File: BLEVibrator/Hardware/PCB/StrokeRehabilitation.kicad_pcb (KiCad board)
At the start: 2 copper layers, 38 x 45 mm, 17 parts, among them P1 JST_PH_01x02, P2 CONN_01X05, Q1 MOSFET_N, SW1 SWITCH_DPDT, U1 TPS737, U2 RFD22301, U3 Brushed_DC_motor

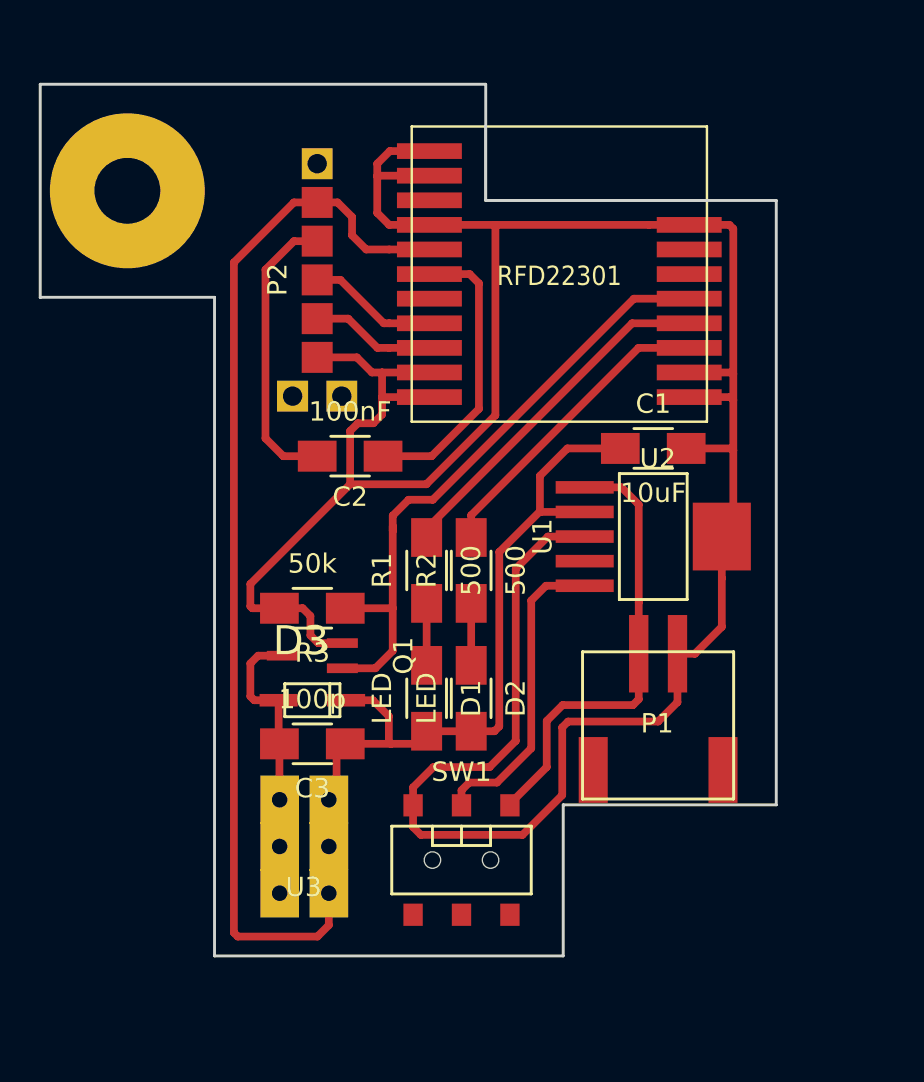
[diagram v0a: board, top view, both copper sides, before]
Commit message: Updated the PCB to have a side-mounted slide switch and connection status LED. The case still needs to be updated to match
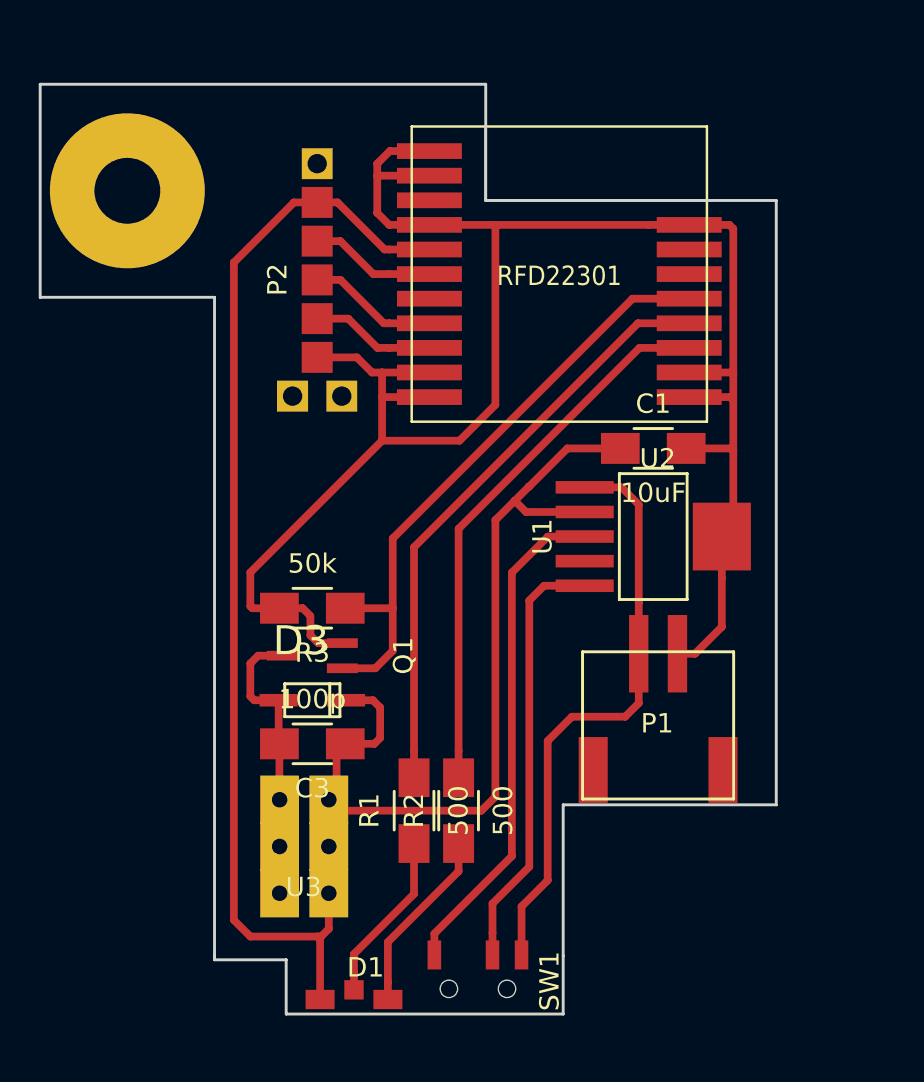
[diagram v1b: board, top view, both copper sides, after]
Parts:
- removed C2: 100nF, FabLibrary:C_1206_HandSoldering_IainEdit
- removed D2: LED, FabLibrary:C_1206_HandSoldering_IainEdit
- D1: value LED -> BI_LED_common_anode; footprint FabLibrary:C_1206_HandSoldering_IainEdit -> IainPersonalLibrary:Bi_LED_SM1204BC-RG
- SW1: value SWITCH_DPDT -> SWITCH_INV; footprint IainPersonalLibrary:SlideSwitch_AYZ0202AGRLC -> IainPersonalLibrary:SlideSwitch_SSSS810701
- moved D1 16.0 mm to (144.8, 146.8), turned to 0 degrees
- moved R1 12.4 mm to (147.8, 137.0)
- moved R2 12.4 mm to (150.2, 137.0)
- moved SW1 6.70 mm to (151.2, 146.2), turned to 0 degrees
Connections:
- D1 pad 1: Net-(D1-Pad1) -> VDD
- D1 pad 2: VDD -> Net-(D1-Pad2)
- P1 pad 1: Net-(C4-Pad2) -> Net-(P1-Pad1)
- P2 pad 2: Net-(C2-Pad2) -> Net-(P2-Pad2)
- R1 pad 1: Net-(D1-Pad1) -> Net-(D1-Pad2)
- R2 pad 1: Net-(D2-Pad1) -> Net-(D1-Pad3)
- SW1 pad 1: Net-(SW1-Pad1) -> GND
- SW1 pad 3: Net-(SW1-Pad3) -> Net-(P1-Pad1)
- U1 pad 1: Net-(C4-Pad2) -> Net-(P1-Pad1)
- U1 pad 5: Net-(SW1-Pad5) -> Net-(SW1-Pad2)
- U2 pad P$14: Net-(C2-Pad1) -> Net-(P2-Pad2)
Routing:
- net Net-(P1-Pad1): track 0.00 -> 30.5 mm
- net Net-(C4-Pad2): track 23.6 -> 0.00 mm
- net Net-(SW1-Pad2): track 0.00 -> 22.3 mm
- net GND: track 150.8 -> 130.7 mm
- net Net-(SW1-Pad5): track 16.0 -> 0.00 mm
- net Net-(C2-Pad1): track 15.2 -> 0.00 mm
- net Net-(C2-Pad2): track 15.0 -> 0.00 mm
- net Net-(R2-Pad2): track 16.0 -> 28.6 mm
- net Net-(R1-Pad2): track 18.4 -> 30.9 mm
- net VDD: track 96.3 -> 106.4 mm
- net Net-(D1-Pad3): track 0.00 -> 9.56 mm
- net Net-(D1-Pad2): track 0.00 -> 8.83 mm
- net Net-(P2-Pad2): track 0.00 -> 6.50 mm
- net Net-(D2-Pad1): track 3.20 -> 0.00 mm
- net Net-(D1-Pad1): track 3.20 -> 0.00 mm
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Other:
- board size 38 x 45 mm -> 38 x 48 mm
- board text added: "GND internally connected in TPS737"

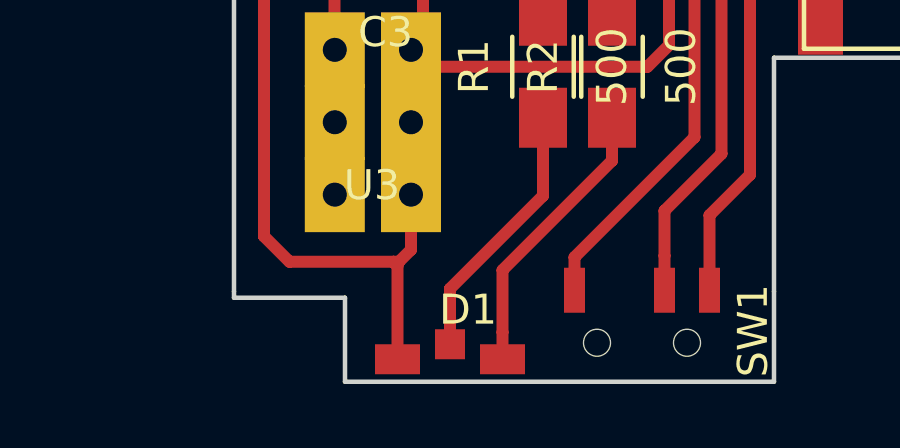
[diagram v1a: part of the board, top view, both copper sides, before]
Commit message: Moved side mount LED back a little bit to make placement and soldering easier
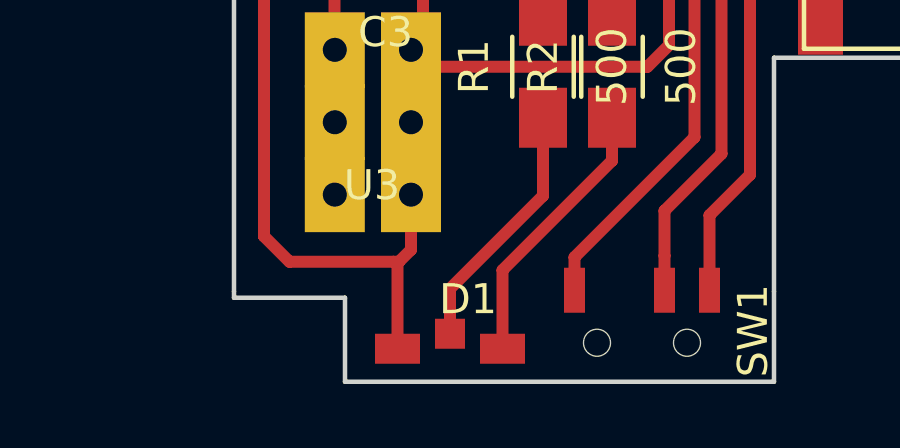
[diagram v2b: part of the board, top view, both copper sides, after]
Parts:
- moved D1 0.35 mm to (144.8, 146.4)
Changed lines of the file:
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@@
     (links 41)
     (no_connects 1)
-    (area 128.474999 99.424999 166.625001 147.575001)
+    (area 128.474999 98.33338 183.342857 151.275)
     (thickness 1.6)
     (drawings 29)
-    (tracks 156)
+    (tracks 154)
     (zones 0)
     (modules 15)
@@
   )
   (module IainPersonalLibrary:Bi_LED_SM1204BC-RG (layer F.Cu)
-    (at 144.75 146.75)
+    (at 144.75 146.4)
     (fp_text reference D1 (at 0.6 -1.65) (layer F.SilkS)
       (effects (font (size 1 1) (thickness 0.15)))
@@
   (gr_line (start 137.55 110.5) (end 128.55 110.5) (angle 90) (layer Edge.Cuts) (width 0.15))
   (gr_line (start 137.55 144.5) (end 137.55 110.5) (angle 90) (layer Edge.Cuts) (width 0.15))
+  (segment (start 143 146.4) (end 143 143.55) (width 0.4) (layer F.Cu) (net 1))
+  (segment (start 143 143.55) (end 143.05 143.5) (width 0.4) (layer F.Cu) (net 1))
   (segment (start 153.05 121) (end 152.05 122) (width 0.4) (layer F.Cu) (net 1))
   (segment (start 152.05 122) (end 152.05 136.280002) (width 0.4) (layer F.Cu) (net 1))
@@
   (segment (start 143.45 143.1) (end 143.05 143.5) (width 0.4) (layer F.Cu) (net 1))
   (segment (start 143.05 143.5) (end 142.863 143.5) (width 0.4) (layer F.Cu) (net 1))
-  (segment (start 142.863 143.5) (end 143 143.637) (width 0.4) (layer F.Cu) (net 1))
-  (segment (start 143 143.637) (end 143 146.75) (width 0.4) (layer F.Cu) (net 1))
   (segment (start 144.3 133.55) (end 145.8 133.55) (width 0.4) (layer F.Cu) (net 1))
   (segment (start 145.8 133.55) (end 146.1 133.25) (width 0.4) (layer F.Cu) (net 1))
@@
   (segment (start 158.56 120.31) (end 156.66 120.31) (width 0.4) (layer F.Cu) (net 15))
   (segment (start 159.45 126.25) (end 159.45 128.9) (width 0.4) (layer F.Cu) (net 15))
-  (segment (start 146.5 145.85) (end 146.5 146.75) (width 0.4) (layer F.Cu) (net 16))
-  (segment (start 146.5 143.781386) (end 146.5 145.85) (width 0.4) (layer F.Cu) (net 16))
+  (segment (start 146.5 143.781386) (end 146.5 146.4) (width 0.4) (layer F.Cu) (net 16))
   (segment (start 150.15 140.131386) (end 146.5 143.781386) (width 0.4) (layer F.Cu) (net 16))
   (segment (start 150.15 138.7) (end 150.15 140.131386) (width 0.4) (layer F.Cu) (net 16))
-  (segment (start 144.75 144.4) (end 144.75 145.35) (width 0.4) (layer F.Cu) (net 17))
+  (segment (start 144.75 144.4) (end 144.75 145.9) (width 0.4) (layer F.Cu) (net 17))
   (segment (start 147.85 138.7) (end 147.85 141.3) (width 0.4) (layer F.Cu) (net 17))
   (segment (start 147.85 141.3) (end 144.75 144.4) (width 0.4) (layer F.Cu) (net 17))
-  (segment (start 144.75 145.35) (end 144.75 146.25) (width 0.4) (layer F.Cu) (net 17))
   (segment (start 142.85 107.6) (end 144.05 107.6) (width 0.4) (layer F.Cu) (net 18))
   (segment (start 144.05 107.6) (end 145.75 109.3) (width 0.4) (layer F.Cu) (net 18))

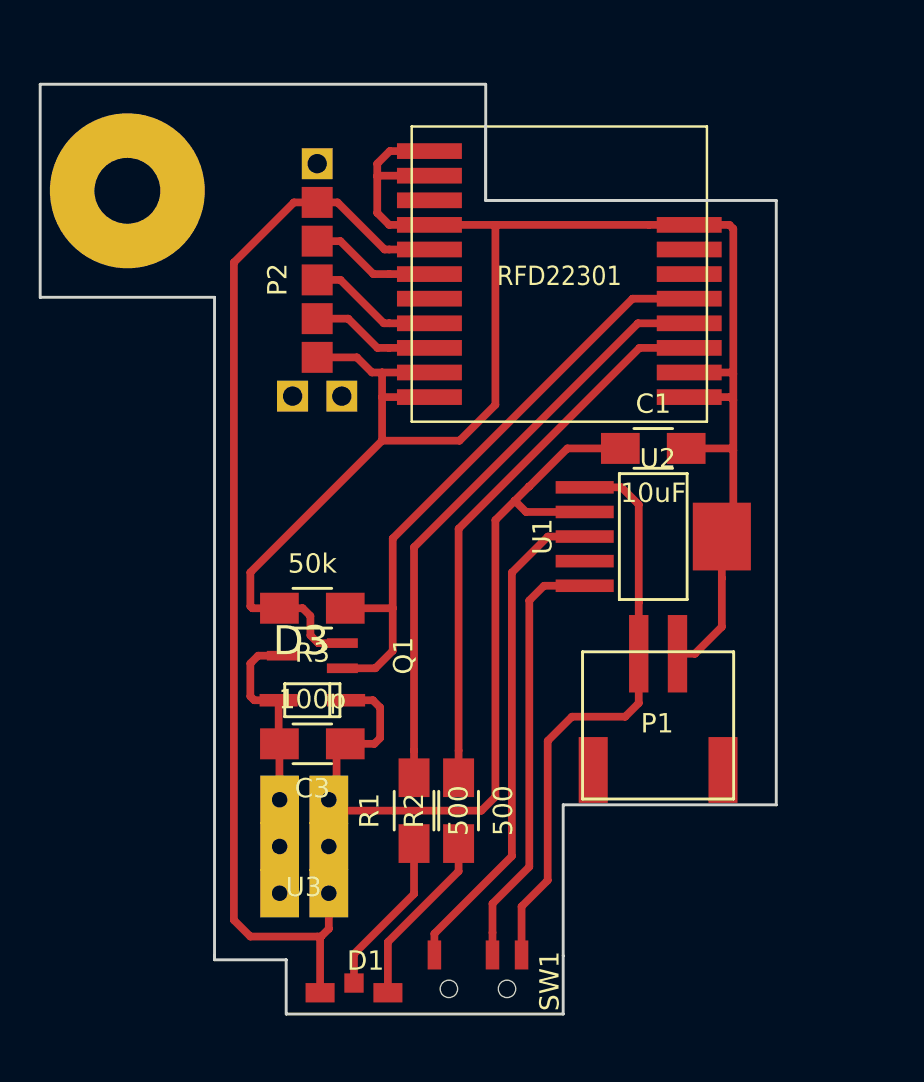
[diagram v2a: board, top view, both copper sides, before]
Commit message: Routed the new PCB. Assigned correct footprints in schematic
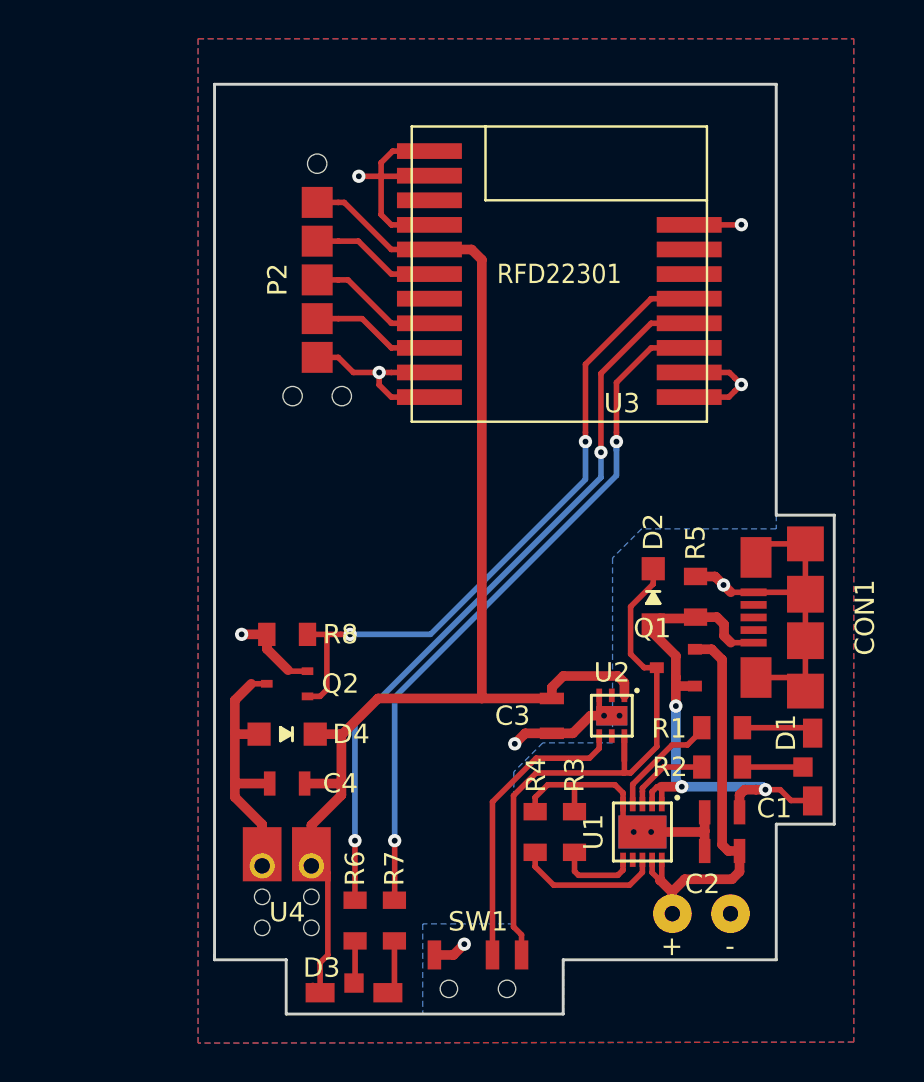
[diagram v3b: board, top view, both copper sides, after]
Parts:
- removed P1: JST_PH_01x02, IainPersonalLibrary:S2B_PH_SM4_TB
- removed REF**: MountHole, FabLibrary:M3_mount_hole
- added BT1: 1S LiPo, IainPersonalLibrary:BatteryCon_WireSolder_0.8mm, F.Cu at (162.7, 142.3)
- added C2: 1uF, IainPersonalLibrary:Murata_capacitor_SMD_0805_reflow, F.Cu at (163.8, 139.1)
- added C4: 100p, IainPersonalLibrary:Murata_capacitor_SMD_0805_reflow, F.Cu at (141.3, 135.6)
- added CON1: USB-MICRO-B, IainPersonalLibrary:Micro_USB_Amphenol_10118192-0001LF, F.Cu at (165.4, 127.0)
- added D2: D_Schottky, IainPersonalLibrary:SOD-123F, F.Cu at (160.2, 126.0)
- added D4: D_Schottky, IainPersonalLibrary:SOD-123F, F.Cu at (141.3, 133.1)
- added Q2: MOSFET_N, IainPersonalLibrary:MCPH3_SOT-323, F.Cu at (141.3, 130.4)
- added R4: 10k, IainPersonalLibrary:Yageo_resistor_SMD_0805_reflow, F.Cu at (154.1, 138.1)
- added R5: 50k, IainPersonalLibrary:Yageo_resistor_SMD_0805_reflow, F.Cu at (162.4, 126.0)
- added R6: 330, IainPersonalLibrary:Yageo_resistor_SMD_0805_reflow, F.Cu at (144.8, 142.7)
- added R7: 330, IainPersonalLibrary:Yageo_resistor_SMD_0805_reflow, F.Cu at (146.8, 142.7)
- added R8: 50k, IainPersonalLibrary:Yageo_resistor_SMD_0805_reflow, F.Cu at (141.3, 127.9)
- added U4: Brushed_DC_motor, IainPersonalLibrary:WireToBoard_1x2_TensionRelief, F.Cu at (140.0, 139.8)
- C1: value 10uF -> 1uF; footprint FabLibrary:C_1206_HandSoldering_IainEdit -> IainPersonalLibrary:Murata_capacitor_SMD_0805_reflow
- C3: value 100p -> 10uF; footprint FabLibrary:C_1206_HandSoldering_IainEdit -> IainPersonalLibrary:Murata_capacitor_SMD_0805_reflow
- D3: value D_Schottky_Small -> BI_LED_common_anode; footprint IainPersonalLibrary:SOD-123_a -> IainPersonalLibrary:Bi_LED_SM1204BC-RG
- P2: value CONN_01X05 -> Programming Header
- Q1: value MOSFET_N -> MOS_P; footprint IainPersonalLibrary:MCPH3_SOT-323 -> IainPersonalLibrary:Vishay_SOT-23
- R1, R2: value 500 -> 330; footprint FabLibrary:C_1206_HandSoldering_IainEdit -> IainPersonalLibrary:Yageo_resistor_SMD_0805_reflow
- R3: value 50k -> 5k; footprint FabLibrary:C_1206_HandSoldering_IainEdit -> IainPersonalLibrary:Yageo_resistor_SMD_0805_reflow
- U1: value TPS737 -> MCP73833; footprint IainPersonalLibrary:SOT-223-5 -> IainPersonalLibrary:MCP73833-XXX_MF
- U2: value RFD22301 -> TPS73701_DRV_6; footprint IainPersonalLibrary:RFD22301_RFDuino -> IainPersonalLibrary:TPS73701_DRV_6
- U3: value Brushed_DC_motor -> RFD22301; footprint IainPersonalLibrary:PrecisionMicrodrives_304_111_Connector_long -> IainPersonalLibrary:RFD22301_RFDuino
- moved U3 31.9 mm to (155.3, 109.3)
- moved D1 26.4 mm to (168.4, 134.7), turned to 90 degrees
- moved U2 23.0 mm to (158.1, 132.1), turned to 270 degrees
- moved C1 19.1 mm to (163.8, 137.1), turned to 180 degrees
- moved Q1 18.8 mm to (161.4, 129.6)
- moved R3 17.8 mm to (156.1, 138.1), turned to 90 degrees
- moved R1 16.5 mm to (163.8, 132.7), turned to 0 degrees
- moved U1 15.3 mm to (159.6, 138.1)
- moved D3 15.3 mm to (144.8, 146.4), turned to 0 degrees
- moved R2 13.8 mm to (163.8, 134.7), turned to 0 degrees
- moved C3 12.4 mm to (155.0, 132.1), turned to 270 degrees
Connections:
- C1 pad 1: VDD -> +5V
- C3 pad 2: Net-(C3-Pad2) -> GND
- D1 pad 1: VDD -> +5V
- D3 pad 2: Net-(C3-Pad2) -> Net-(D3-Pad2)
- Q1 pad D: Net-(C3-Pad2) -> Net-(D2-Pad1)
- Q1 pad G: motor -> +5V
- Q1 pad S: GND -> +BATT
- R1 pad 1: Net-(D1-Pad2) -> Net-(R1-Pad1)
- R1 pad 2: Net-(R1-Pad2) -> Net-(D1-Pad3)
- R2 pad 1: Net-(D1-Pad3) -> Net-(R2-Pad1)
- R2 pad 2: Net-(R2-Pad2) -> Net-(D1-Pad2)
- R3 pad 1: motor -> Net-(R3-Pad1)
- SW1 pad 3: Net-(P1-Pad1) -> Net-(D2-Pad1)
- U1 pad 1: Net-(P1-Pad1) -> +5V
- U1 pad 2: VDD -> +5V
- U1 pad 3: GND -> Net-(R2-Pad1)
- U1 pad 4: Net-(U1-Pad4) -> Net-(R1-Pad1)
- U1 pad 5: Net-(SW1-Pad2) -> GND
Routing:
- net GND: track 130.7 -> 77.4 mm, vias 0 -> 8
- net Net-(R6-Pad2): track 0.00 -> 38.1 mm, vias 0 -> 2
- net VDD: track 106.0 -> 68.0 mm
- net Net-(R7-Pad2): track 0.00 -> 36.5 mm, vias 0 -> 2
- net Net-(R1-Pad2): track 30.9 -> 0.00 mm
- net Net-(D2-Pad1): track 0.00 -> 30.7 mm
- net Net-(P1-Pad1): track 30.5 -> 0.00 mm
- net +5V: track 0.00 -> 28.8 mm, vias 0 -> 3
- net Net-(R2-Pad2): track 28.6 -> 0.00 mm
- net +BATT: track 0.00 -> 21.6 mm
- net Net-(C3-Pad2): track 15.0 -> 0.00 mm
- net Net-(C4-Pad2): track 0.00 -> 13.6 mm
- net Net-(R4-Pad1): track 0.00 -> 7.59 mm
- net Net-(SW1-Pad2): track 22.3 -> 15.2 mm
- net Net-(R1-Pad1): track 0.00 -> 5.89 mm
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- added copper zone on B.Cu, net GND
- added copper zone on F.Cu, net GND
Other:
- board size 38 x 48 mm -> 32 x 48 mm
- net class Default: clearance 0.4 -> 0.2; trace_width 0.4 -> 0.29; via_dia 0.6 -> 0.6858; via_drill 0.4 -> 0.3
- net class HighCurrent added: clearance 0.2, trace_width 0.5, via_dia 0.6858, via_drill 0.3
- net class Minimum added: clearance 0.1524, trace_width 0.1524, via_dia 0.508, via_drill 0.3
- net class Small added: clearance 0.2, trace_width 0.29, via_dia 0.6858, via_drill 0.3
- rule trace_clearance: 0.4 -> 0.2
- rule trace_min: 0.4 -> 0.1524
- rule via_min_size: 0.4 -> 0.508
- board text removed: "GND internally connected in TPS737"
